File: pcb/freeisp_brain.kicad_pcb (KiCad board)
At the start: 2 copper layers, 100 x 100 mm, 26 parts, among them J1 12V IN, J10 BUZZER, J11 HORN, J12 SENSE, J13 BOOST IN+ IN- OUT+ OUT-, J4 TFT, J5 RC522, J7 REED, J8 LED R, J9 LED G, K1 HORN RLY, U1 BUCK IN+ IN- OUT+ OUT-, U2 CHARGER IN+ IN- B+ B-, U3A ESP32 L, U3B ESP32 R, U4 MPU-6050

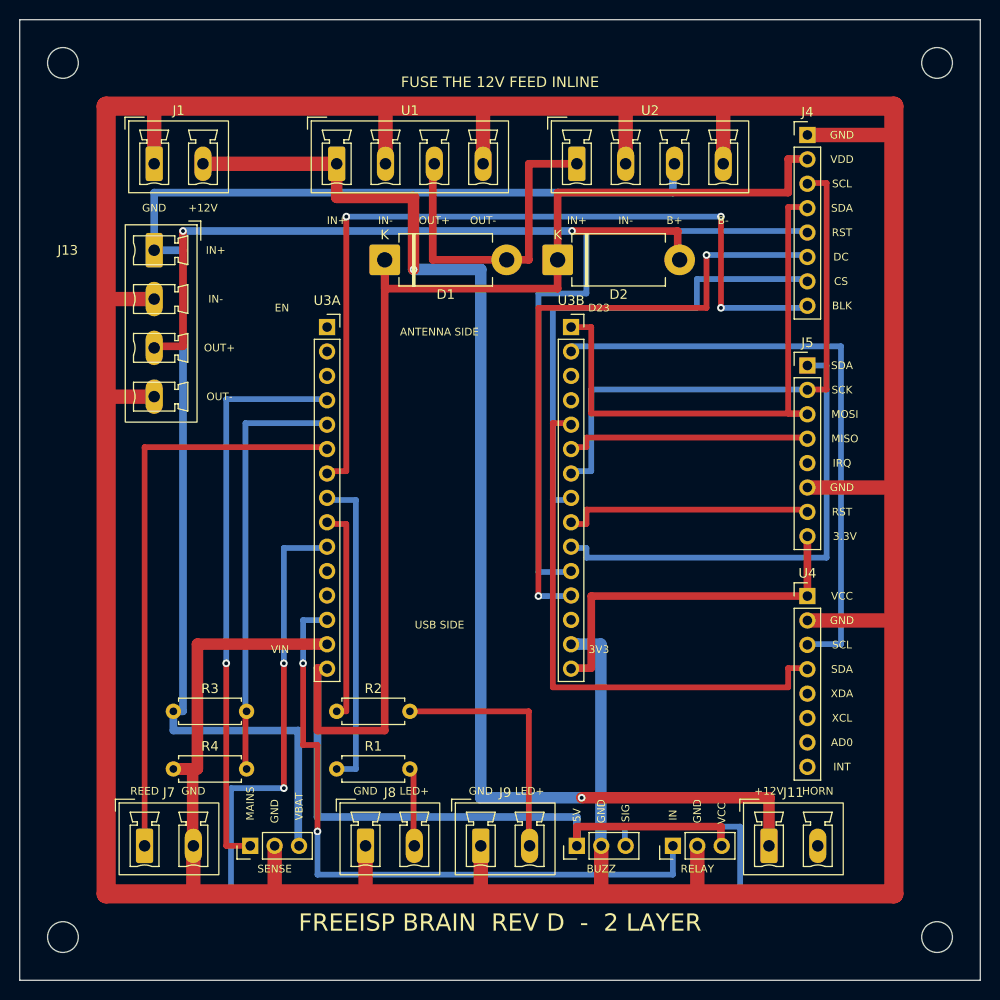
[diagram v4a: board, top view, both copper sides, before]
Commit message: Rev E: fix both critical review findings + all majors, re-verified clean
Francis caught C1 himself and demanded an independent reviewer; the review
(fresh-eyes agent, adversarial brief) confirmed it and found C2:

C1  J12 "MAINS" was a bare field pin wired straight into GPIO34 (3.3V max,
    input-only, no clamp) - a factory-printed invitation to destroy the
    chip. FIXED: J12 deleted entirely. Mains presence is sensed on-board
    from the +12V rail through R5/R6 (100k/27k -> 2.55V) + C3 100n. No
    terminal above 3.3V can reach a GPIO any more.

C2  J11's horn return (HORN_RET) was a single-pad net connected to NOTHING
    - the horn could never sound, and both my audit (skips <2-pad nets) and
    KiCad (one-pad nets have no ratsnest) reported it as fine. FIXED: J11
    pin 2 is GND; the full horn loop is documented in PINOUT.md.

M1  Buck must be set to 5.4-5.5V, not 5.0V, so mains always wins the
    diode-OR and the TP4056 can terminate charge (doc change).
M2  D3 1N5822 in series after J1 = reverse-polarity protection; J1 pin
    order flipped to +12V-GND to match PSU convention.
Minors: C1 470uF bulk on 5V_SYS, C2/C3 100n on both ADC dividers (source-
    impedance smoothing), R7 1k relay-drive series (opto backfeed), R8 1k
    reed series. VBAT no longer appears on any field pin.

Why the originals were missed, recorded in README: DRC and audit.py verify
that the copper matches the netlist; neither can ask what voltage a
technician will put on a terminal, or notice a net with one pad. Circuit-
level independent review is now a standing step before any order.

Re-verified: audit.py PASS (no crossings, no sub-clearance pairs, every
net one island), KiCad DRC 0 errors 0 unconnected, renders inspected.
Board is rev E; fitcheck_1to1.pdf and PINOUT.md regenerated to match.

Co-Authored-By: Claude Opus 5 (1M context) <noreply@anthropic.com>
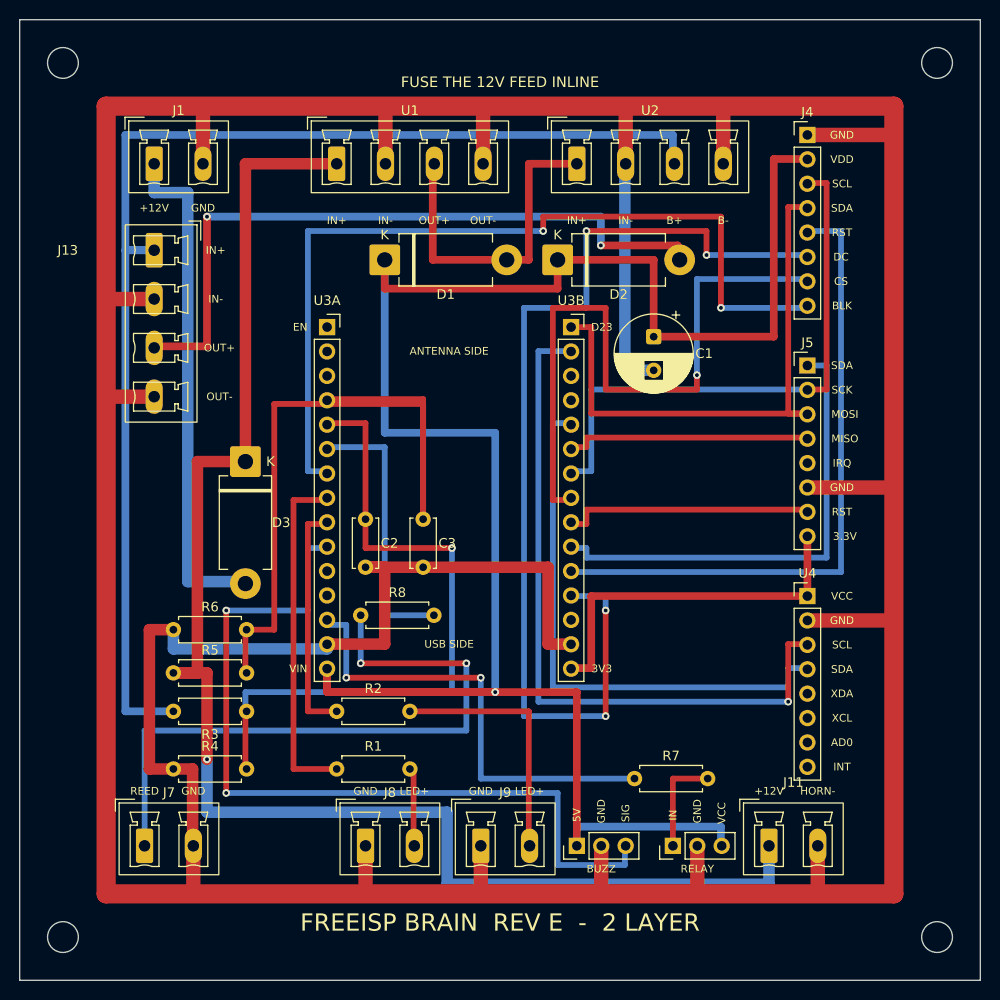
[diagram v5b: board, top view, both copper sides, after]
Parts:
- removed J12: SENSE, Connector_PinHeader_2.54mm:PinHeader_1x03_P2.54mm_Vertical
- added C1: 470u, Capacitor_THT:CP_Radial_D8.0mm_P3.50mm, F.Cu at (126.0, 73.0)
- added C2: 100n, Capacitor_THT:C_Disc_D5.0mm_W2.5mm_P5.00mm, F.Cu at (96.0, 92.0)
- added C3: 100n, Capacitor_THT:C_Disc_D5.0mm_W2.5mm_P5.00mm, F.Cu at (102.0, 92.0)
- added D3: 1N5822, Diode_THT:D_DO-201AD_P12.70mm_Horizontal, F.Cu at (83.5, 86.0)
- added R5: 100k, Resistor_THT:R_Axial_DIN0207_L6.3mm_D2.5mm_P7.62mm_Horizontal, F.Cu at (76.0, 108.0)
- added R6: 27k, Resistor_THT:R_Axial_DIN0207_L6.3mm_D2.5mm_P7.62mm_Horizontal, F.Cu at (76.0, 103.5)
- added R7: 1k, Resistor_THT:R_Axial_DIN0207_L6.3mm_D2.5mm_P7.62mm_Horizontal, F.Cu at (124.0, 119.0)
- added R8: 1k, Resistor_THT:R_Axial_DIN0207_L6.3mm_D2.5mm_P7.62mm_Horizontal, F.Cu at (95.5, 102.0)
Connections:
- J1 pad 1: GND -> +12V_IN
- J1 pad 2: +12V -> GND
- J11 pad 2: HORN_RET -> GND
- J7 pad 1: REED -> REED_F
- K1 pad 1: HORN_IN -> HORN_DRV
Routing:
- net REED_F: track 0.00 -> 68.5 mm, vias 0 -> 2
- net GND: track 488.1 -> 542.9 mm
- net +12V_IN: track 0.00 -> 53.0 mm
- net TFT_DC: track 66.9 -> 107.1 mm, vias 2 -> 4
- net BUZZ: track 119.0 -> 87.0 mm
- net REED: track 60.5 -> 28.7 mm
- net +12V: track 129.9 -> 158.0 mm, vias 2 -> 1
- net +5V_SYS: track 189.5 -> 216.4 mm, vias 0 -> 1
- net SENSE_BATT: track 44.6 -> 70.6 mm, vias 0 -> 1
- net HORN_IN: track 70.5 -> 48.5 mm
- net SENSE_MAINS: track 59.5 -> 80.9 mm, vias 1 -> 0
- net TFT_CS: track 51.5 -> 68.5 mm, vias 0 -> 1
- net VBAT: track 142.0 -> 131.0 mm
- net SCL: track 63.1 -> 73.9 mm, vias 0 -> 1
- net HORN_DRV: track 0.00 -> 10.6 mm
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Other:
- board text added: "FREEISP BRAIN REV E - 2 LAYER"
- board text added: "HORN-"
- board text removed: "FREEISP BRAIN REV D - 2 LAYER"
- board text removed: "HORN"
- board text removed: "MAINS"
- board text removed: "SENSE"
- board text removed: "VBAT"

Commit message: Horn moved to 5V_SYS: works on battery, can never see 12V
Francis checked his actual horn: it is a 3-5V type, not the 12V unit in the
old BOM. That resolves the reviewer's battery-mode concern the right way
round - as built, J11 would have fed the 3-5V horn raw 12V and destroyed
it on first trigger.

J11 pin 1 is now +5V_SYS (silk "+5V"): the horn rides the diode-OR rail,
so it keeps sounding on battery after a mains cut, and 12V can no longer
reach it. The 12V net now feeds only the buck and the sense divider.

PINOUT updated: explicit note that the PCB does not switch the horn (K1 is
control pins only; the relay module's COM/NO screw terminals do the
switching - Francis's reading, confirmed correct), a loud warning that a
future 12V horn is a board change not a wiring change, and boost module
sizing >=2A since battery mode now carries the sounding horn too.

Re-verified: audit PASS, DRC 0 errors, 0 unconnected.

Co-Authored-By: Claude Opus 5 (1M context) <noreply@anthropic.com>
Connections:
- J11 pad 1: +12V -> +5V_SYS
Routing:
- net +12V: track 158.0 -> 70.0 mm, vias 1 -> 0
- net +5V_SYS: track 216.4 -> 221.3 mm
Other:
- board text added: "+5V"
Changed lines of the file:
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@@
 			(remove_unused_layers no)
 			(roundrect_rratio 0.138889)
-			(net 6 "+12V")
+			(net 4 "+5V_SYS")
 		)
 		(pad "2" thru_hole oval
@@
 	)
 	(segment
+		(start 133.0800 126.0000)
+		(end 138.0000 126.0000)
+		(width 0.8)
+		(layer "F.Cu")
+		(net 4)
+	)
+	(segment
 		(start 96.0000 97.0000)
 		(end 102.0000 97.0000)
@@
 		(net 26)
 	)
-	(segment
-		(start 76.0000 108.0000)
-		(end 79.5000 108.0000)
-		(width 1.2)
-		(layer "F.Cu")
-		(net 6)
-	)
-	(segment
-		(start 79.5000 108.0000)
-		(end 79.5000 117.0000)
-		(width 1.2)
-		(layer "F.Cu")
-		(net 6)
-	)
-	(segment
-		(start 79.5000 117.0000)
-		(end 79.5000 122.5000)
-		(width 1.2)
-		(layer "B.Cu")
-		(net 6)
-	)
-	(segment
-		(start 79.5000 122.5000)
-		(end 104.5000 122.5000)
-		(width 1.2)
-		(layer "B.Cu")
-		(net 6)
-	)
-	(segment
-		(start 104.5000 122.5000)
-		(end 104.5000 130.0000)
-		(width 1.2)
-		(layer "B.Cu")
-		(net 6)
-	)
-	(segment
-		(start 104.5000 130.0000)
-		(end 138.0000 130.0000)
-		(width 1.2)
-		(layer "B.Cu")
-		(net 6)
-	)
-	(segment
-		(start 138.0000 130.0000)
-		(end 138.0000 126.0000)
-		(width 1.2)
-		(layer "B.Cu")
-		(net 6)
-	)
 	(via
 		(at 105.0000 95.0000)
@@
 		(net 26)
 	)
-	(via
-		(at 79.5000 117.0000)
-		(size 0.8)
-		(drill 0.4)
-		(layers "F.Cu" "B.Cu")
-		(net 6)
-	)
 	(gr_text "FREEISP BRAIN  REV E  -  2 LAYER"
 		(at 110.0000 134.0000)
@@
 		)
 	)
-	(gr_text "+12V"
+	(gr_text "+5V"
 		(at 138.0000 120.3000)
 		(layer "F.SilkS")

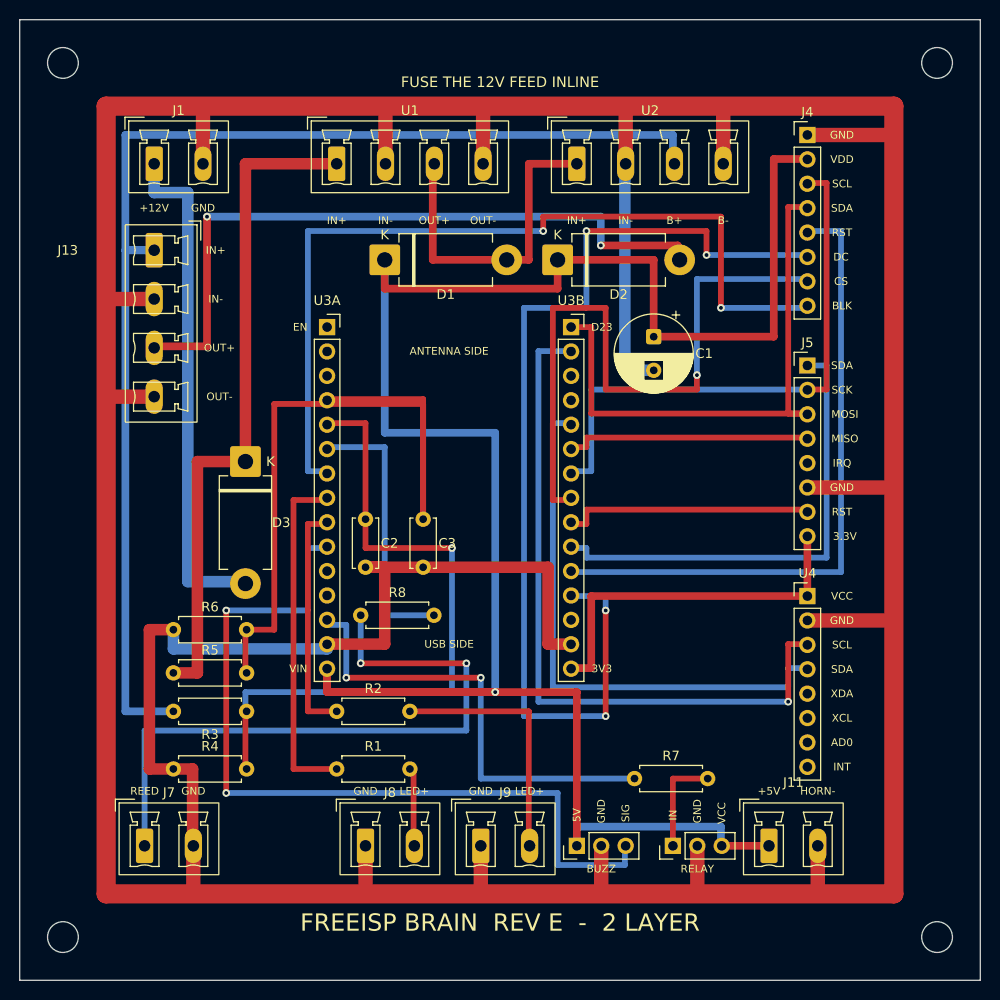
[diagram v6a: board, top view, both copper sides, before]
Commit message: Charger terminal is OUT+/OUT- not B+/B-; set-points on silk; silk clean
From Francis's wiring verdict, one item was a board error not an assembly
note: the protected TP4056's load must hang on OUT+/OUT- (behind the DW01
FETs). The U2 terminal was silk-labelled B+/B- - instructing an unprotected
discharge path. Relabelled OUT+/OUT-; the 18650 wires straight to the
module's own B+/B- pads and never touches the board. Nets unchanged.

Also:
- Buck/boost set-points now printed on the board's top edge ("SET BUCK
  5.4V - BOOST 5.0V") - the 0.4V offset IS the diode-OR priority mechanism
  Francis asked about, and the values can no longer get lost in a doc.
- J11 reference moved out of the U4/HORN- silk pinch: silk_overlap now 0.
  Remaining warnings: 33 embedded-footprint metadata + 8 J13-rotation
  artifacts (its own body art over its own pads; fab auto-clips). The "140
  warnings" figure was a stale DRC report from two revisions back.
- PINOUT: match-by-printed-name assembly block (relay pin order varies,
  TP4056 OUT vs B, buzzer SIG 3.3V, TFT 8-pin order, trimmers set first).
- FreeISP_Box.ino marked SUPERSEDED (comment-only banner, not compiled):
  its placeholder pins (LEDs on GPIO6/7 = flash pins) must never be flashed
  against this PCB. The board follows LiveDashboardNext + CardDisarm.

Verified: audit PASS, DRC 0 errors, 0 unconnected.

Co-Authored-By: Claude Opus 5 (1M context) <noreply@anthropic.com>
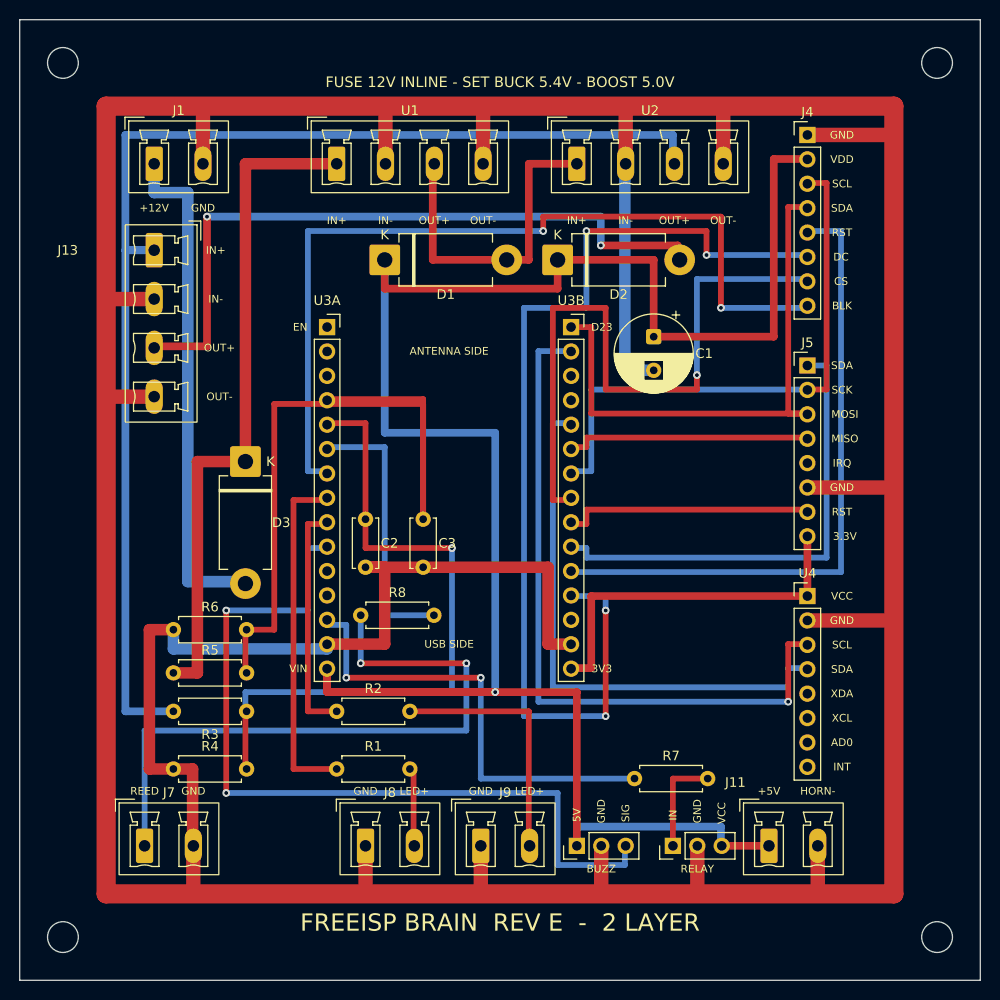
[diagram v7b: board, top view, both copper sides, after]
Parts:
- U2: value CHARGER IN+ IN- B+ B- -> CHARGER IN+ IN- OUT+ OUT-
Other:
- board text added: "FUSE 12V INLINE - SET BUCK 5.4V - BOOST 5.0V"
- board text removed: "B+"
- board text removed: "B-"
- board text removed: "FUSE THE 12V FEED INLINE"
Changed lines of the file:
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@@
 		(tags "phoenix_contact connector MCV_01x02_G_5.08mm")
 		(property "Reference" "J11"
-			(at 2.54 -6.60 0)
+			(at -3.50 -6.60 0)
 			(layer "F.SilkS")
 			(effects
@@
 			)
 		)
-		(property "Value" "CHARGER  IN+ IN- B+ B-"
+		(property "Value" "CHARGER  IN+ IN- OUT+ OUT-"
 			(at 7.62 4.1 0)
 			(layer "F.Fab")
@@
 		)
 	)
-	(gr_text "FUSE THE 12V FEED INLINE"
+	(gr_text "FUSE 12V INLINE - SET BUCK 5.4V - BOOST 5.0V"
 		(at 110.0000 46.5000)
 		(layer "F.SilkS")
@@
 		)
 	)
-	(gr_text "B+"
+	(gr_text "OUT+"
 		(at 128.1600 60.9000)
 		(layer "F.SilkS")
@@
 		)
 	)
-	(gr_text "B-"
+	(gr_text "OUT-"
 		(at 133.2400 60.9000)
 		(layer "F.SilkS")

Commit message: Rev F: the real board is the 38-pin DevKitC, not the 30-pin V1
Francis counted his devkit: 19 pins per side. The whole board was drawn for
the 30-pin DevKit V1 - caught by asking the question BEFORE ordering, which
is exactly what the paper-test gate exists for. His photo of the board
sitting on the rev-D print also confirms the standard DevKitC pin order
(GND 23 22 TX RX 21 GND 19 18 5... readable on the module silkscreen).

Changes:
- Sockets are 1x19 (48.3mm), anchored at y=28; pin maps U3A/U3B fully
  remapped to the DevKitC order. Same GPIOs, new positions: 3V3 is now
  top-LEFT, 5V bottom-left, GND top-right.
- Six FLASH pins (SD0-SD3, CMD, CLK = GPIO6-11) now exist as holes and are
  verified UNCONNECTED, along with strap pins D0/D15 and TX0/RX0 - 20
  no-connects checked by trace.py.
- The longer sockets displaced D1 (down), D2+C1 (vertical, right of U3B,
  respaced twice to reopen the TFT_DC corridor) and R1/R2 (x36).
- Row spacing stays 25.4mm (DevKitC standard) - vernier check pending.

All three checks green: audit PASS, trace PASS (98 connections, 20
no-connects), DRC 0 errors 0 unconnected. PINOUT rewritten for 19+19.

Co-Authored-By: Claude Opus 5 (1M context) <noreply@anthropic.com>
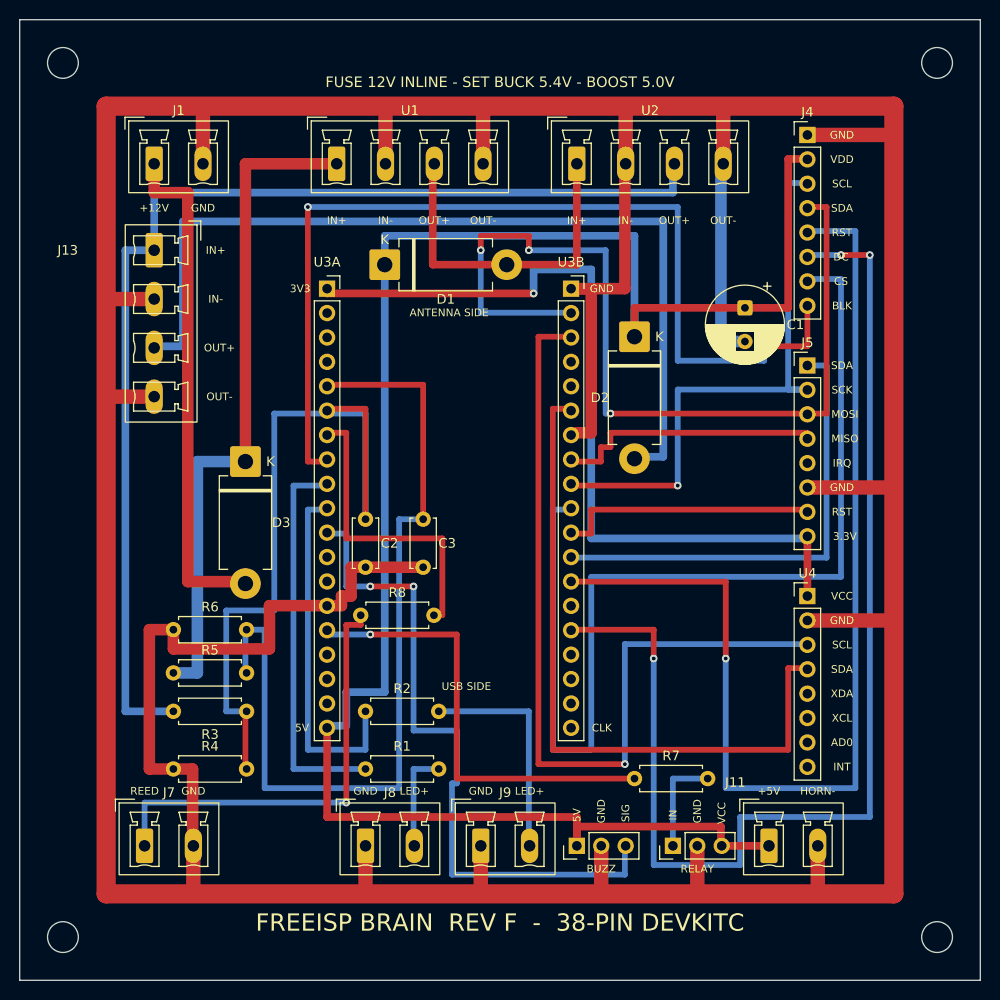
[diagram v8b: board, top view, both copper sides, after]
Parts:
- removed the U3A at (92.0, 72.0)
- removed the U3B at (117.4, 72.0)
- added U3A: ESP32 L, Connector_PinSocket_2.54mm:PinSocket_1x19_P2.54mm_Vertical, F.Cu at (92.0, 68.0)
- added U3B: ESP32 R, Connector_PinSocket_2.54mm:PinSocket_1x19_P2.54mm_Vertical, F.Cu at (117.4, 68.0)
- moved D2 11.3 mm to (124.0, 73.0), turned to 270 degrees
- moved C1 9.96 mm to (135.5, 70.0)
- moved R1 3.00 mm to (96.0, 118.0)
- moved R2 3.00 mm to (96.0, 112.0)
- moved D1 0.50 mm to (98.0, 65.5)
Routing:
- net +3V3: track 38.3 -> 87.3 mm, vias 0 -> 1
- net TFT_RST: track 67.1 -> 114.1 mm, vias 0 -> 1
- net TFT_CS: track 68.5 -> 109.5 mm, vias 1 -> 0
- net MOSI: track 59.1 -> 95.4 mm, vias 0 -> 3
- net +5V_SYS: track 221.3 -> 192.3 mm, vias 1 -> 0
- net REED_F: track 68.5 -> 46.5 mm, vias 2 -> 1
- net +5V_BAT: track 72.6 -> 93.6 mm, vias 2 -> 0
- net TFT_DC: track 107.1 -> 125.6 mm, vias 4 -> 3
- net BUZZ: track 87.0 -> 70.5 mm
- net SDA: track 57.9 -> 72.5 mm
- net SCL: track 73.9 -> 88.4 mm
- net LED_G: track 24.5 -> 37.0 mm
- net TFT_BLK: track 90.1 -> 102.3 mm
- net VBAT: track 131.0 -> 119.0 mm
- net SENSE_MAINS: track 80.9 -> 91.4 mm
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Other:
- board text added: "CLK"
- board text added: "FREEISP BRAIN REV F - 38-PIN DEVKITC"
- board text removed: "D23"
- board text removed: "EN"
- board text removed: "FREEISP BRAIN REV E - 2 LAYER"
- board text removed: "VIN"
